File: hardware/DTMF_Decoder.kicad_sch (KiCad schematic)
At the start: 38 parts

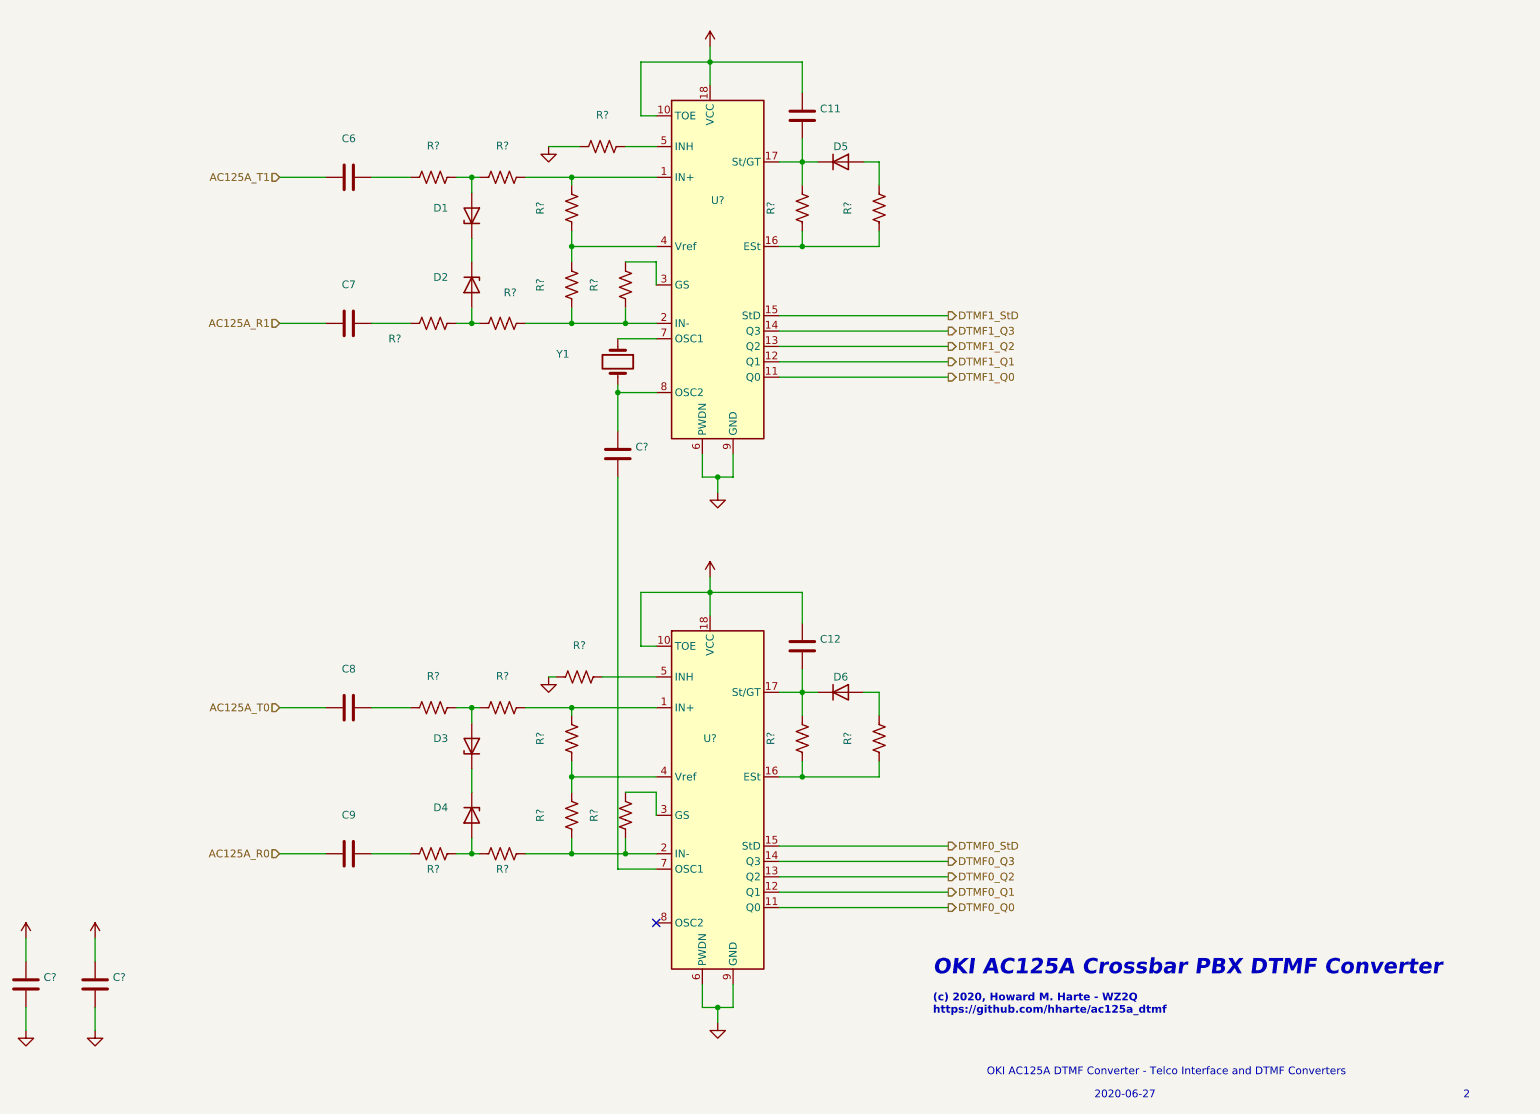
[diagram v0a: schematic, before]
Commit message: Fix a couple DRC errors in the layout.
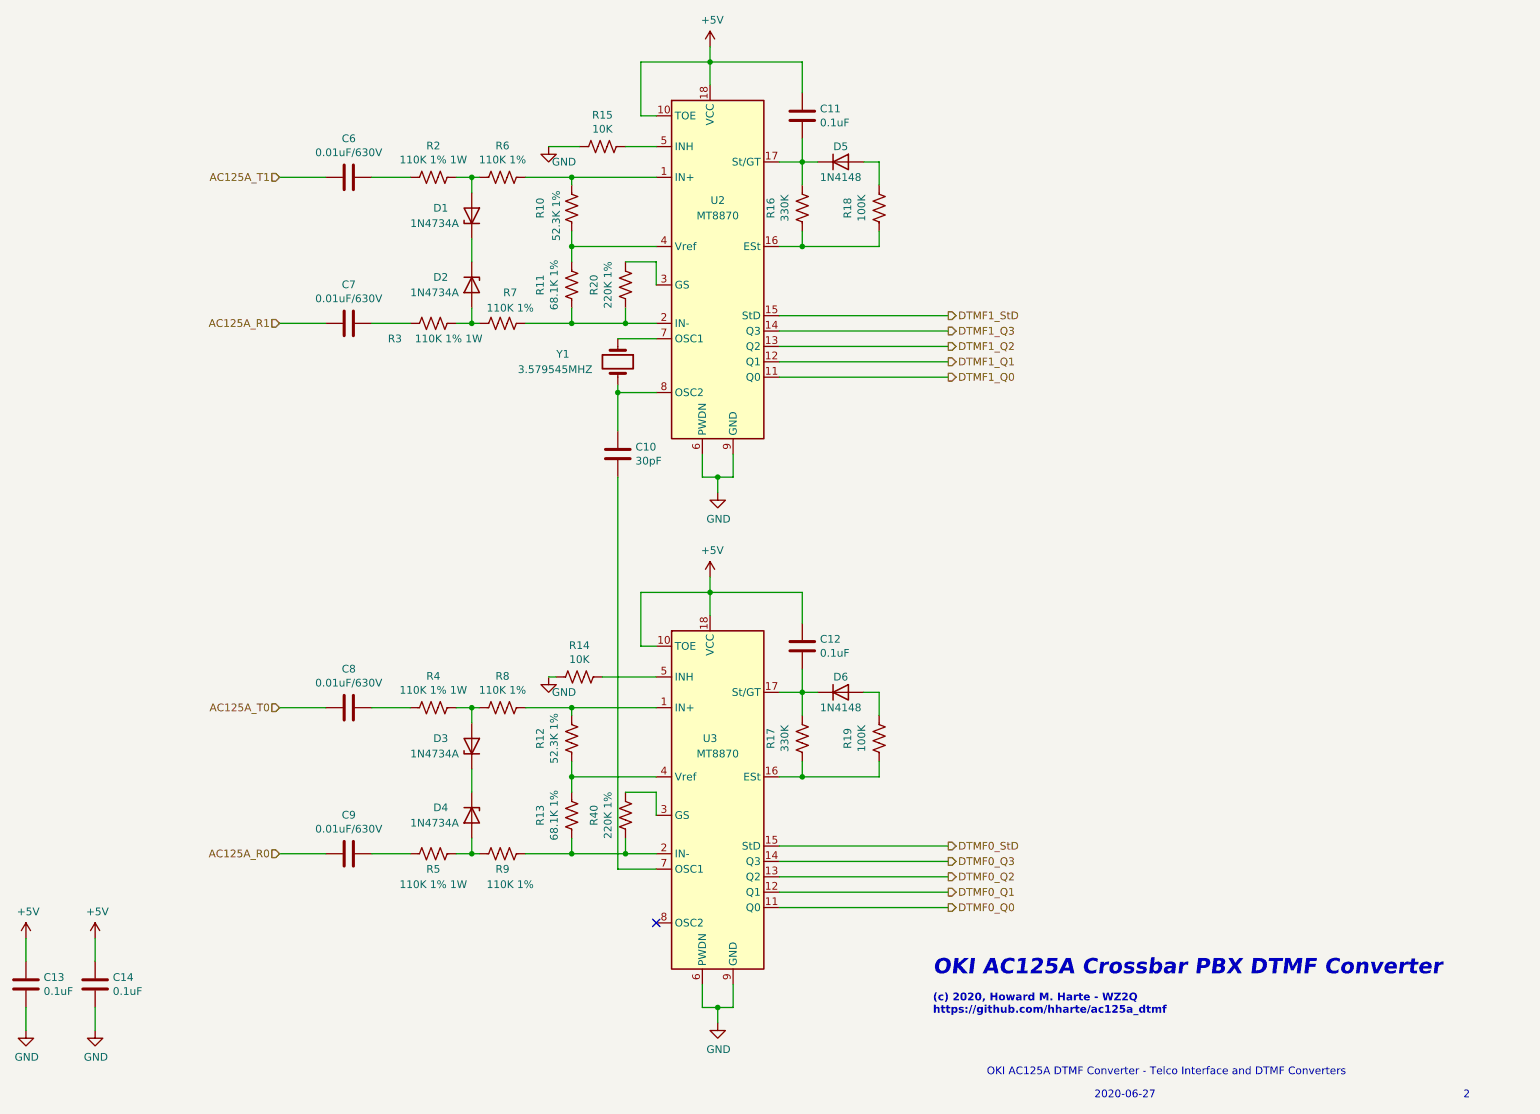
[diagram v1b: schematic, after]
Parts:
- C10: renamed from C?; value (none) -> 30pF; footprint (none) -> Capacitor_THT:C_Disc_D3.0mm_W2.0mm_P2.50mm
- C11, C12: value (none) -> 0.1uF; footprint (none) -> Capacitor_THT:C_Disc_D3.0mm_W2.0mm_P2.50mm
- C13, C14: renamed from C?; value (none) -> 0.1uF; footprint (none) -> Capacitor_THT:C_Disc_D3.0mm_W2.0mm_P2.50mm
- C6, C7, C8, C9: value (none) -> 0.01uF/630V; footprint (none) -> Capacitor_THT:C_Disc_D7.5mm_W5.0mm_P5.00mm
- D1, D2, D3, D4: value (none) -> 1N4734A; footprint (none) -> Diode_THT:D_DO-41_SOD81_P7.62mm_Horizontal
- D5, D6: value (none) -> 1N4148; footprint (none) -> Diode_THT:D_DO-35_SOD27_P7.62mm_Horizontal
- R10, R12: renamed from R?; value (none) -> 52.3K 1%; footprint (none) -> Resistor_THT:R_Axial_DIN0207_L6.3mm_D2.5mm_P7.62mm_Horizontal
- R11, R13: renamed from R?; value (none) -> 68.1K 1%; footprint (none) -> Resistor_THT:R_Axial_DIN0207_L6.3mm_D2.5mm_P7.62mm_Horizontal
- R14, R15: renamed from R?; value (none) -> 10K; footprint (none) -> Resistor_THT:R_Axial_DIN0207_L6.3mm_D2.5mm_P7.62mm_Horizontal
- R16, R17: renamed from R?; value (none) -> 330K; footprint (none) -> Resistor_THT:R_Axial_DIN0207_L6.3mm_D2.5mm_P7.62mm_Horizontal
- R18, R19: renamed from R?; value (none) -> 100K; footprint (none) -> Resistor_THT:R_Axial_DIN0207_L6.3mm_D2.5mm_P7.62mm_Horizontal
- R2, R3, R4, R5: renamed from R?; value (none) -> 110K 1% 1W; footprint (none) -> Resistor_THT:R_Axial_DIN0207_L6.3mm_D2.5mm_P7.62mm_Horizontal
- R20, R40: renamed from R?; value (none) -> 220K 1%; footprint (none) -> Resistor_THT:R_Axial_DIN0207_L6.3mm_D2.5mm_P7.62mm_Horizontal
- R6, R7, R8, R9: renamed from R?; value (none) -> 110K 1%; footprint (none) -> Resistor_THT:R_Axial_DIN0207_L6.3mm_D2.5mm_P7.62mm_Horizontal
- U2, U3: renamed from U?; value (none) -> MT8870; footprint (none) -> Package_DIP:DIP-18_W7.62mm
- Y1: value (none) -> 3.579545MHZ; footprint (none) -> Crystal:Crystal_HC49-U_Vertical
